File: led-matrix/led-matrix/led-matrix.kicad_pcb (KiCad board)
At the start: 4 copper layers, 88.9 x 77.5 mm, 303 parts, among them J1 Conn_2Rows-05Pins, J2 Conn_2Rows-05Pins, Q1 2N7002, Q10 2N7002, Q11 2N7002, Q12 2N7002, Q13 2N7002, Q14 2N7002, Q15 2N7002, Q16 2N7002, Q2 2N7002, Q3 2N7002, Q4 2N7002, Q5 2N7002, Q6 2N7002, Q7 2N7002, Q8 2N7002, Q9 2N7002, U1 74LS595, U2 74LS595, U3 74LS595, U4 74LS595, U5 AMS1117-3.3

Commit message: Updated layout
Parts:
- moved C3 359.8 mm to (322.6, 135.4), turned to 90 degrees
- moved C2 350.0 mm to (302.3, 135.1), turned to 90 degrees
- moved U4 344.5 mm to (315.0, 134.6), turned to 90 degrees
- moved U3 343.7 mm to (295.9, 134.6), turned to 90 degrees
- moved C1 188.0 mm to (142.2, 121.9)
- moved U1 188.0 mm to (142.2, 114.3)
- moved Q13 180.3 mm to (246.4, 176.3), turned to 90 degrees
- moved R13 175.7 mm to (246.4, 171.4), turned to 90 degrees
- moved Q14 166.4 mm to (254.0, 182.9), turned to 90 degrees
- moved Q16 163.7 mm to (266.7, 177.8), turned to 90 degrees
- moved R14 163.4 mm to (254.0, 179.1), turned to 90 degrees
- moved R16 163.1 mm to (269.2, 173.2), turned to 90 degrees
- moved C4 160.3 mm to (142.2, 91.4), turned to 0 degrees
- moved U2 153.7 mm to (142.2, 85.1), turned to 0 degrees
- moved Q12 153.5 mm to (238.8, 186.7), turned to 90 degrees
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
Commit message: Updated layout
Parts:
- J1, J2: moved to B.Cu
- moved U3 197.5 mm to (101.6, 99.1)
- moved C2 197.5 mm to (108.0, 99.5)
- moved C3 197.5 mm to (128.3, 99.8)
- moved U4 197.5 mm to (120.7, 99.1)
- moved Q12 132.3 mm to (133.3, 106.7), turned to 270 degrees
- moved Q14 131.4 mm to (146.1, 108.0), turned to 270 degrees
- moved Q16 130.3 mm to (157.5, 106.7), turned to 270 degrees
- moved R16 130.0 mm to (154.9, 111.3), turned to 270 degrees
- moved Q13 127.3 mm to (139.7, 106.9), turned to 270 degrees
- moved R14 127.2 mm to (146.1, 111.8), turned to 270 degrees
- moved Q15 126.5 mm to (151.1, 107.7), turned to 270 degrees
- moved R12 126.5 mm to (133.3, 111.8), turned to 270 degrees
- moved R11 124.7 mm to (127.0, 110.5), turned to 270 degrees
- moved Q10 124.5 mm to (120.7, 106.7), turned to 270 degrees
- moved Q11 123.8 mm to (127.0, 105.7), turned to 270 degrees
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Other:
- board size 88.9 x 77.5 mm -> 105.4 x 101.6 mm

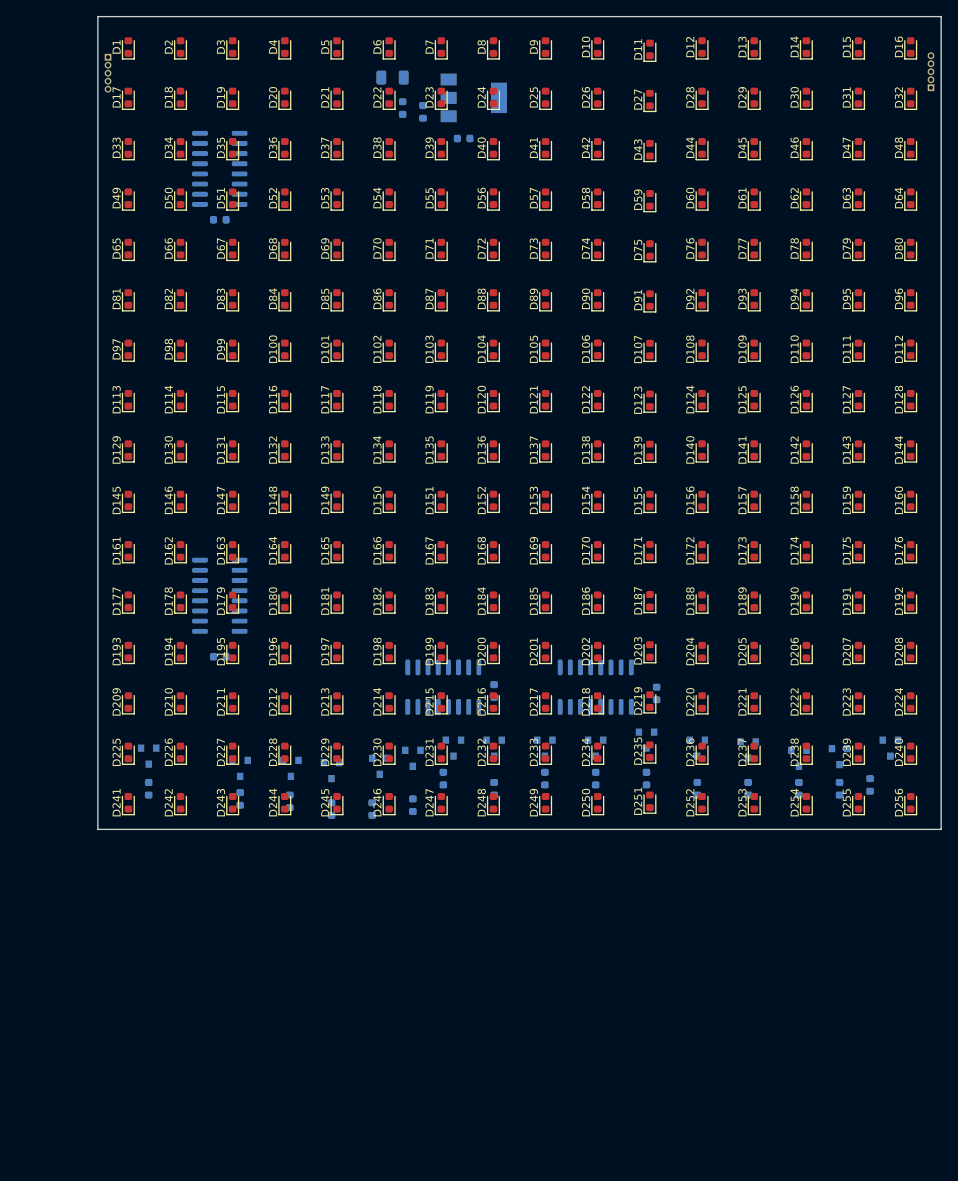
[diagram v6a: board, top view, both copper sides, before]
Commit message: Updated schematic and layout
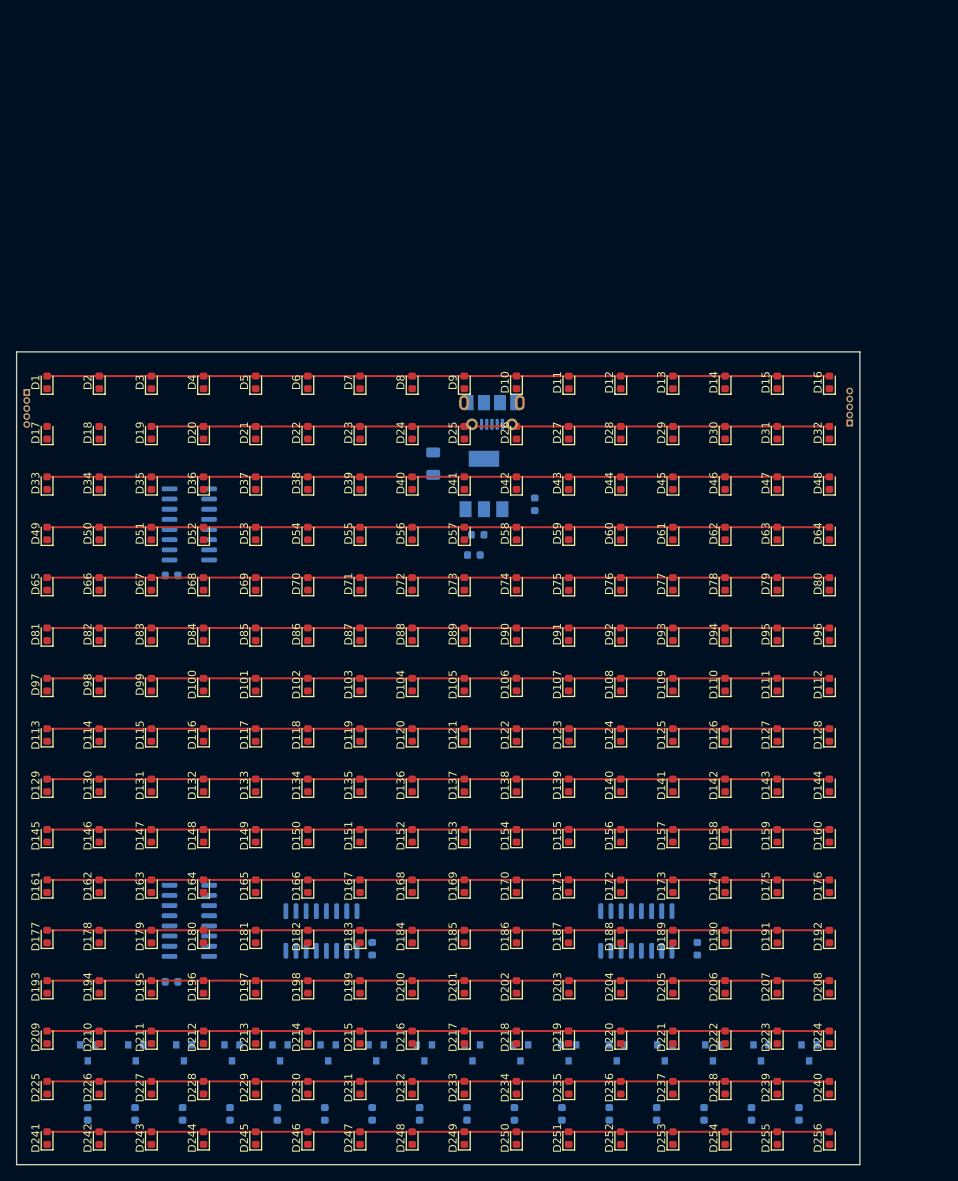
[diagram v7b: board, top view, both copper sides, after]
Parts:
- added J3: USB_B_Micro, Connector_USB:USB_Micro-B_Molex-105017-0001, B.Cu at (107.7, 64.7)
- moved C6 56.6 mm to (105.4, 82.5), turned to 0 degrees
- moved D257 53.3 mm to (105.9, 80.0), turned to 180 degrees
- moved F1 48.5 mm to (100.3, 71.1), turned to 90 degrees
- moved U5 48.3 mm to (106.7, 73.7), turned to 90 degrees
- moved C5 46.6 mm to (113.0, 76.2), turned to 270 degrees
- moved C4 44.9 mm to (67.6, 85.1)
- moved U2 44.6 mm to (69.8, 78.7)
- moved D251 43.3 mm to (117.3, 155.4)
- moved D235 43.3 mm to (117.3, 149.1)
- moved D219 43.2 mm to (117.3, 142.8)
- moved R11 43.2 mm to (116.4, 152.4)
- moved D203 43.2 mm to (117.3, 136.5)
- moved D187 43.2 mm to (117.3, 130.2)
- moved D171 43.1 mm to (117.3, 123.9)
- moved R10 43.1 mm to (110.5, 152.4)
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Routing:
- net ROW4: track 0.00 -> 97.8 mm
- net ROW3: track 0.00 -> 97.8 mm
- net ROW0: track 0.00 -> 97.8 mm
- net ROW2: track 0.00 -> 97.8 mm
- net ROW5: track 0.00 -> 97.8 mm
- net ROW9: track 0.00 -> 97.8 mm
- net ROW8: track 0.00 -> 97.8 mm
- net ROW7: track 0.00 -> 97.8 mm
- net ROW6: track 0.00 -> 97.8 mm
- net ROW15: track 0.00 -> 97.8 mm
- net ROW14: track 0.00 -> 97.8 mm
- net ROW12: track 0.00 -> 97.8 mm
- net ROW11: track 0.00 -> 97.8 mm
- net ROW10: track 0.00 -> 97.8 mm
- net ROW13: track 0.00 -> 97.6 mm
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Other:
- copper layers 4 -> 2

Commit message: Minor
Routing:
- net Net-(D1-Pad1): track 0.00 -> 9.91 mm, vias 0 -> 2
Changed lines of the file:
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@@
     (thickness 1.6)
     (drawings 4)
-    (tracks 125)
+    (tracks 132)
     (zones 0)
     (modules 304)
@@
     (34 B.Paste user)
     (35 F.Paste user)
-    (36 B.SilkS user hide)
-    (37 F.SilkS user hide)
-    (38 B.Mask user hide)
-    (39 F.Mask user hide)
-    (40 Dwgs.User user hide)
-    (41 Cmts.User user hide)
-    (42 Eco1.User user hide)
-    (43 Eco2.User user hide)
-    (44 Edge.Cuts user hide)
+    (36 B.SilkS user)
+    (37 F.SilkS user)
+    (38 B.Mask user)
+    (39 F.Mask user)
+    (40 Dwgs.User user)
+    (41 Cmts.User user)
+    (42 Eco1.User user)
+    (43 Eco2.User user)
+    (44 Edge.Cuts user)
     (45 Margin user)
     (46 B.CrtYd user)
@@
     (via_min_size 0.4)
     (via_min_drill 0.3)
+    (blind_buried_vias_allowed yes)
     (uvia_size 0.3)
     (uvia_drill 0.1)
@@
     (aux_axis_origin 0 0)
     (grid_origin 58.42 116.84)
-    (visible_elements FFEDFF67)
+    (visible_elements FFFDFF6F)
     (pcbplotparams
       (layerselection 0x010fc_ffffffff)
@@
   (segment (start 129.826996 66.47) (end 110.743997 66.47) (width 0.25) (layer F.Cu) (net 3))
   (segment (start 130.301996 66.47) (end 129.826996 66.47) (width 0.25) (layer F.Cu) (net 3))
+  (segment (start 52.07 61.7475) (end 52.07 63.5) (width 0.25) (layer F.Cu) (net 4))
+  (segment (start 52.07 63.5) (end 52.07 63.5) (width 0.25) (layer F.Cu) (net 4))
+  (via blind (at 52.07 63.5) (size 0.8) (drill 0.4) (layers F.Cu B.Cu) (net 4))
+  (segment (start 52.07 63.5) (end 52.07 68.58) (width 0.25) (layer B.Cu) (net 4))
+  (segment (start 52.07 68.58) (end 52.07 69.85) (width 0.25) (layer B.Cu) (net 4))
+  (via micro (at 52.07 69.85) (size 0.8) (drill 0.4) (layers F.Cu B.Cu) (net 4))
+  (segment (start 52.07 69.85) (end 52.07 68.045) (width 0.25) (layer F.Cu) (net 4))
   (segment (start 52.07 85.3625) (end 58.589333 85.3625) (width 0.25) (layer F.Cu) (net 16))
   (segment (start 58.589333 85.3625) (end 65.108666 85.3625) (width 0.25) (layer F.Cu) (net 16))
